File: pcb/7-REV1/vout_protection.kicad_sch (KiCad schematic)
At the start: 21 parts, among them Q3 PMXB56EN, Q4 PMXB56EN, Q6 2N7002KT, U17 LM393BIDSGR

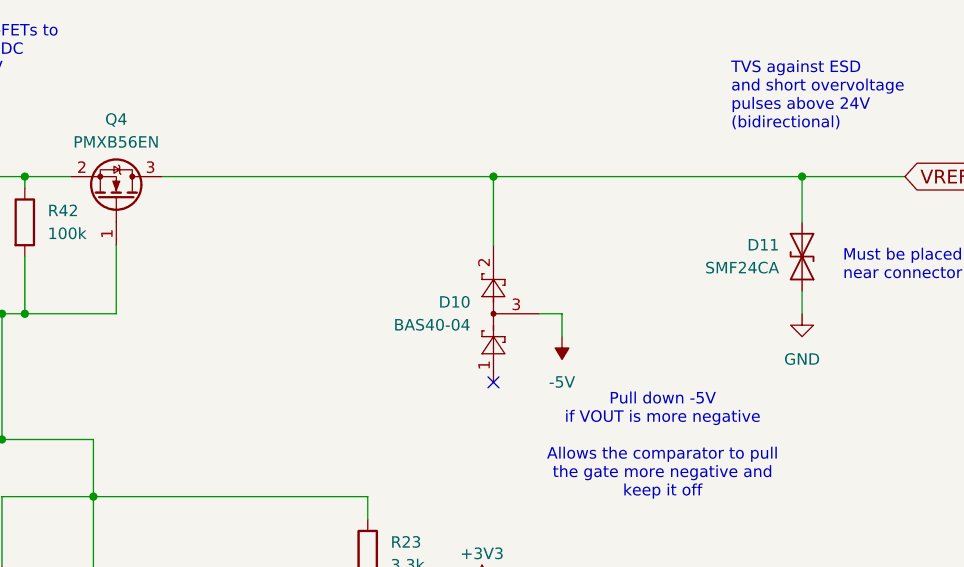
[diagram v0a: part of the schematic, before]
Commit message: use a 1N4148WT instead of BAS40-04 in the VOUT protection
- used to pull low the aux voltage when the external voltage is lower than -5V
- SOD-523 is smaller than SOT-523
- The BAS40-04 was easier blown in ESD/surge tests.
  Placement solved this, but the 1N4148WT will be more resilient
- The increased forward voltage shouldn't matter, we must just go low enough to not turn on the FETs
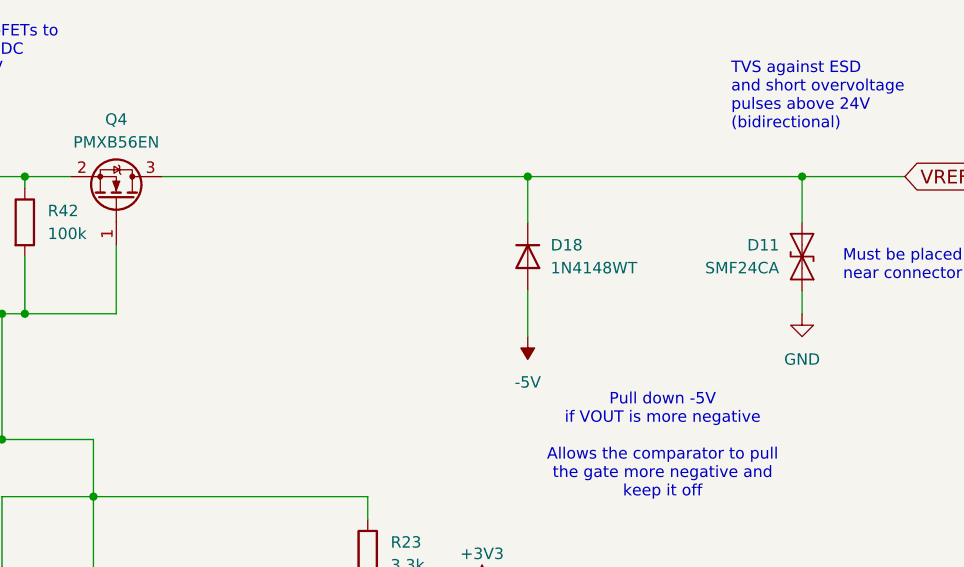
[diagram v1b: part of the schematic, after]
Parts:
- removed D10: BAS40-04, Package_TO_SOT_SMD:SOT-523, symbol Diode:BAS40-04
- added D18: 1N4148WT, Diode_SMD:D_SOD-523, symbol Diode:1N4148WS
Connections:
- net -5V: now also D18.2 (A)
- net VREF_VOUT: now also D18.1 (K)
- no-connect marks 2 -> 1
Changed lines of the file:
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@@
 	)
 	(junction
-		(at 204.47 48.26)
-		(diameter 0)
-		(color 0 0 0 0)
-	)
-	(junction
 		(at 160.02 83.82)
 		(diameter 0)
@@
 	)
 	(junction
+		(at 208.28 48.26)
+		(diameter 0)
+		(color 0 0 0 0)
+	)
+	(junction
 		(at 40.64 142.24)
 		(diameter 0)
@@
 		(at 97.79 163.83)
 	)
-	(no_connect
-		(at 204.47 71.12)
-	)
 	(wire
 		(pts
@@
 	(wire
 		(pts
-			(xy 204.47 48.26) (xy 238.76 48.26)
-		)
-		(stroke
-			(width 0)
-			(type default)
-		)
-	)
-	(wire
-		(pts
 			(xy 238.76 60.96) (xy 238.76 63.5)
 		)
@@
 	(wire
 		(pts
-			(xy 167.64 48.26) (xy 204.47 48.26)
+			(xy 167.64 48.26) (xy 208.28 48.26)
 		)
 		(stroke
@@
 	(wire
 		(pts
+			(xy 208.28 48.26) (xy 238.76 48.26)
+		)
+		(stroke
+			(width 0)
+			(type default)
+		)
+	)
+	(wire
+		(pts
 			(xy 152.4 48.26) (xy 152.4 49.53)
 		)
@@
 	(wire
 		(pts
-			(xy 212.09 63.5) (xy 212.09 66.04)
+			(xy 208.28 60.96) (xy 208.28 66.04)
 		)
 		(stroke
@@
 	(wire
 		(pts
-			(xy 99.06 48.26) (xy 105.41 48.26)
+			(xy 208.28 48.26) (xy 208.28 53.34)
 		)
 		(stroke
@@
 	(wire
 		(pts
-			(xy 27.94 160.02) (xy 27.94 161.29)
+			(xy 99.06 48.26) (xy 105.41 48.26)
 		)
 		(stroke
@@
 	(wire
 		(pts
-			(xy 105.41 48.26) (xy 129.54 48.26)
+			(xy 27.94 160.02) (xy 27.94 161.29)
 		)
 		(stroke
@@
 	(wire
 		(pts
-			(xy 209.55 63.5) (xy 212.09 63.5)
+			(xy 105.41 48.26) (xy 129.54 48.26)
 		)
 		(stroke
@@
 	(wire
 		(pts
-			(xy 204.47 48.26) (xy 204.47 55.88)
-		)
-		(stroke
-			(width 0)
-			(type default)
-		)
-	)
-	(wire
-		(pts
 			(xy 152.4 48.26) (xy 157.48 48.26)
 		)
@@
 	)
 	(symbol
-		(lib_id "Diode:BAS40-04")
-		(at 207.01 63.5 90)
-		(unit 1)
-		(exclude_from_sim no)
-		(in_bom yes)
-		(on_board yes)
-		(dnp no)
-		(property "Reference" "D10"
-			(at 201.93 62.2299 90)
-			(effects
-				(font
-					(size 1.27 1.27)
-				)
-				(justify left)
-			)
-		)
-		(property "Value" "BAS40-04"
-			(at 201.93 64.7699 90)
-			(effects
-				(font
-					(size 1.27 1.27)
-				)
-				(justify left)
-			)
-		)
-		(property "Footprint" "Package_TO_SOT_SMD:SOT-523"
-			(at 199.39 69.85 0)
-			(effects
-				(font
-					(size 1.27 1.27)
-				)
-				(justify left)
-				(hide yes)
-			)
-		)
-		(property "Datasheet" "http://www.vishay.com/docs/85701/bas40v.pdf"
-			(at 204.47 66.548 0)
-			(effects
-				(font
-					(size 1.27 1.27)
-				)
-				(hide yes)
-			)
-		)
-		(property "Description" "40V 0.2A Dual Small Signal Schottky Diodes"
-			(at 207.01 63.5 0)
-			(effects
-				(font
-					(size 1.27 1.27)
-				)
-				(hide yes)
-			)
-		)
-		(property "Description_1" ""
-			(at 207.01 63.5 0)
-			(effects
-				(font
-					(size 1.27 1.27)
-				)
-				(hide yes)
-			)
-		)
-		(property "MAXIMUM_PACKAGE_HEIGHT" ""
-			(at 207.01 63.5 0)
-			(effects
-				(font
-					(size 1.27 1.27)
-				)
-				(hide yes)
-			)
-		)
-		(property "PARTREV" ""
-			(at 207.01 63.5 0)
-			(effects
-				(font
-					(size 1.27 1.27)
-				)
-				(hide yes)
-			)
-		)
-		(property "STANDARD" ""
-			(at 207.01 63.5 0)
-			(effects
-				(font
-					(size 1.27 1.27)
-				)
-				(hide yes)
-			)
-		)
-		(pin "1"
-		)
-		(pin "3"
-		)
-		(pin "2"
-		)
-		(instances
-			(project "7-REV1"
-				(path "/1f56410a-eaac-4444-b0f7-cfd3531e22ac/95c5ca91-1e6b-49a9-86b2-64918a8e6404"
-					(reference "D10")
-					(unit 1)
-				)
-			)
-		)
-	)
-	(symbol
 		(lib_id "Device:D_TVS")
 		(at 143.51 55.88 90)
@@
 	)
 	(symbol
+		(lib_id "Diode:1N4148WS")
+		(at 208.28 57.15 270)
+		(unit 1)
+		(exclude_from_sim no)
+		(in_bom yes)
+		(on_board yes)
+		(dnp no)
+		(property "Reference" "D18"
+			(at 210.82 55.88 90)
+			(effects
+				(font
+					(size 1.27 1.27)
+				)
+				(justify left)
+			)
+		)
+		(property "Value" "1N4148WT"
+			(at 210.82 58.42 90)
+			(effects
+				(font
+					(size 1.27 1.27)
+				)
+				(justify left)
+			)
+		)
+		(property "Footprint" "Diode_SMD:D_SOD-523"
+			(at 203.835 57.15 0)
+			(effects
+				(font
+					(size 1.27 1.27)
+				)
+				(hide yes)
+			)
+		)
+		(property "Datasheet" "https://www.vishay.com/docs/85751/1n4148ws.pdf"
+			(at 208.28 57.15 0)
+			(effects
+				(font
+					(size 1.27 1.27)
+				)
+				(hide yes)
+			)
+		)
+		(property "Description" ""
+			(at 208.28 57.15 0)
+			(effects
+				(font
+					(size 1.27 1.27)
+				)
+				(hide yes)
+			)
+		)
+		(property "RMB" "0.182079"
+			(at 208.28 57.15 0)
+			(effects
+				(font
+					(size 1.27 1.27)
+				)
+				(hide yes)
+			)
+		)
+		(property "Supplier" "https://item.szlcsc.com/120141.html"
+			(at 208.28 57.15 0)
+			(effects
+				(font
+					(size 1.27 1.27)
+				)
+				(hide yes)
+			)
+		)
+		(property "Description_1" ""
+			(at 208.28 57.15 0)
+			(effects
+				(font
+					(size 1.27 1.27)
+				)
+				(hide yes)
+			)
+		)
+		(property "MAXIMUM_PACKAGE_HEIGHT" ""
+			(at 208.28 57.15 0)
+			(effects
+				(font
+					(size 1.27 1.27)
+				)
+				(hide yes)
+			)
+		)
+		(property "PARTREV" ""
+			(at 208.28 57.15 0)
+			(effects
+				(font
+					(size 1.27 1.27)
+				)
+				(hide yes)
+			)
+		)
+		(property "STANDARD" ""
+			(at 208.28 57.15 0)
+			(effects
+				(font
+					(size 1.27 1.27)
+				)
+				(hide yes)
+			)
+		)
+		(pin "1"
+		)
+		(pin "2"
+		)
+		(instances
+			(project "7-REV1"
+				(path "/1f56410a-eaac-4444-b0f7-cfd3531e22ac/95c5ca91-1e6b-49a9-86b2-64918a8e6404"
+					(reference "D18")
+					(unit 1)
+				)
+			)
+		)
+	)
+	(symbol
 		(lib_id "power:-5V")
 		(at 40.64 161.29 180)
@@
 	(symbol
 		(lib_id "power:-5V")
-		(at 212.09 66.04 180)
+		(at 208.28 66.04 180)
 		(unit 1)
 		(exclude_from_sim no)
@@
 		(fields_autoplaced yes)
 		(property "Reference" "#PWR094"
-			(at 212.09 62.23 0)
+			(at 208.28 62.23 0)
 			(effects
 				(font
@@
 		)
 		(property "Value" "-5V"
-			(at 212.09 71.12 0)
+			(at 208.28 71.12 0)
 			(effects
 				(font
@@
 		)
 		(property "Footprint" ""
-			(at 212.09 66.04 0)
+			(at 208.28 66.04 0)
 			(effects
 				(font
@@
 		)
 		(property "Datasheet" ""
-			(at 212.09 66.04 0)
+			(at 208.28 66.04 0)
 			(effects
 				(font
@@
 		)
 		(property "Description" "Power symbol creates a global label with name \"-5V\""
-			(at 212.09 66.04 0)
+			(at 208.28 66.04 0)
 			(effects
 				(font

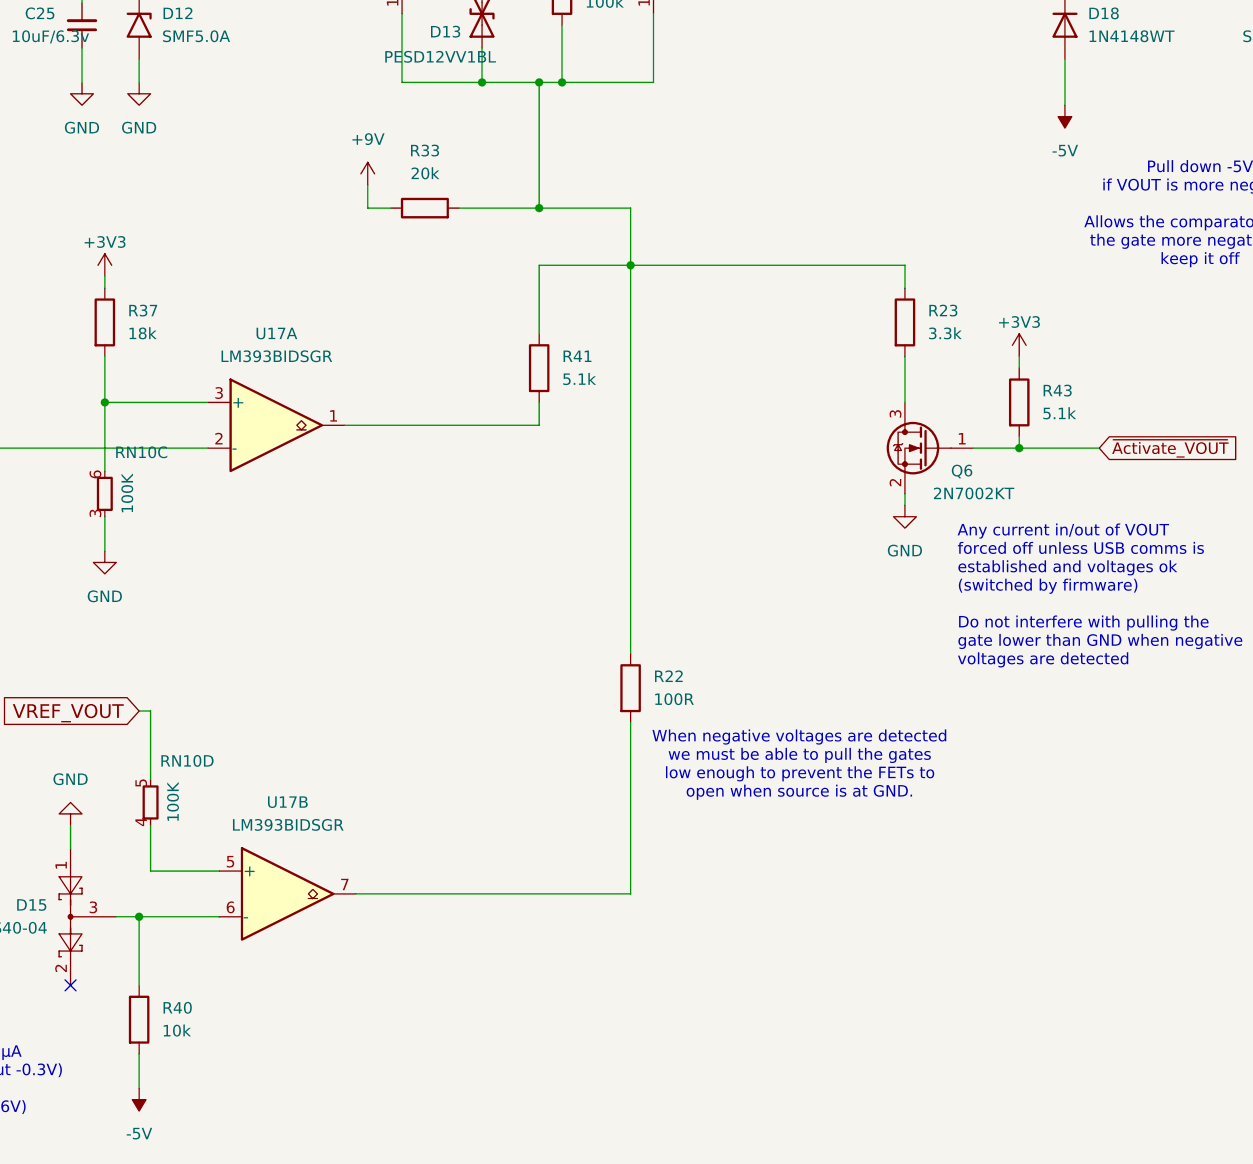
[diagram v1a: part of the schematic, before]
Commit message: change resistor naming from k to K to unify BOM lines
change the gate pullup resistor from 20k to 18k to remove one BOM line
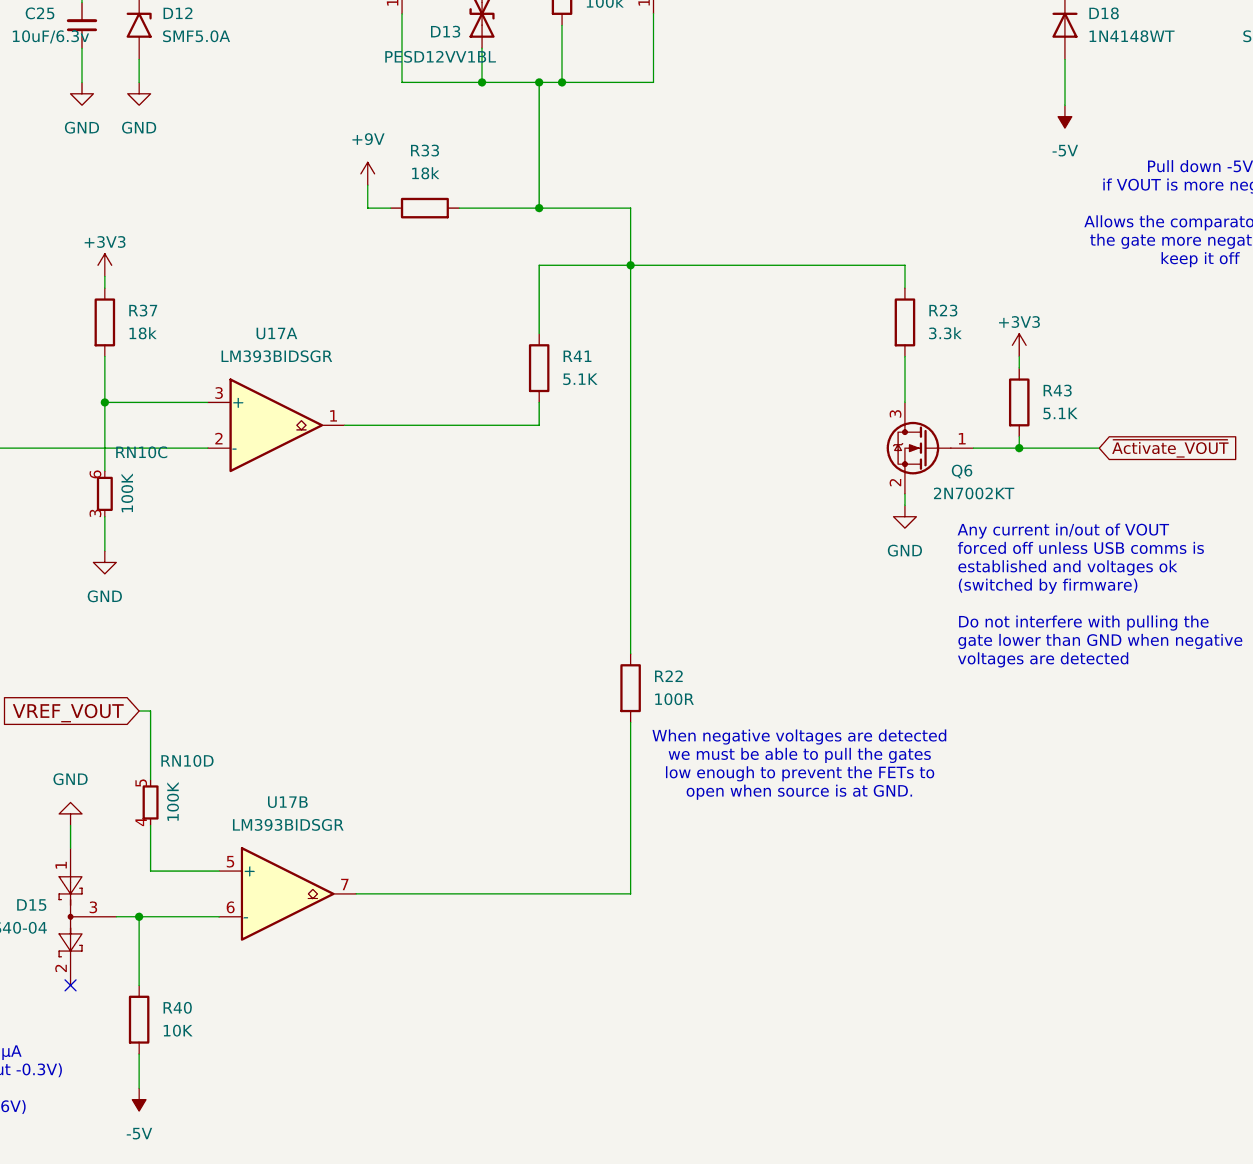
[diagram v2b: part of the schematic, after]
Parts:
- R33: value 20k -> 18k
- R40: value 10k -> 10K
- R41, R43: value 5.1k -> 5.1K
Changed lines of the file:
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@@
 			)
 		)
-		(property "Value" "10k"
+		(property "Value" "10K"
 			(at 107.95 168.9099 0)
 			(effects
@@
 			)
 		)
-		(property "Value" "5.1k"
+		(property "Value" "5.1K"
 			(at 205.74 100.3299 0)
 			(effects
@@
 			)
 		)
-		(property "Value" "5.1k"
+		(property "Value" "5.1K"
 			(at 152.4 96.5199 0)
 			(effects
@@
 			)
 		)
-		(property "Value" "20k"
+		(property "Value" "18k"
 			(at 137.16 73.66 90)
 			(effects
